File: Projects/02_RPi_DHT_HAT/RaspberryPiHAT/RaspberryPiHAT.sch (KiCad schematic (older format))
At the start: 7 parts, among them J1 Raspberry_Pi_2_3, SW1 SW_DPST, U1 DHT22

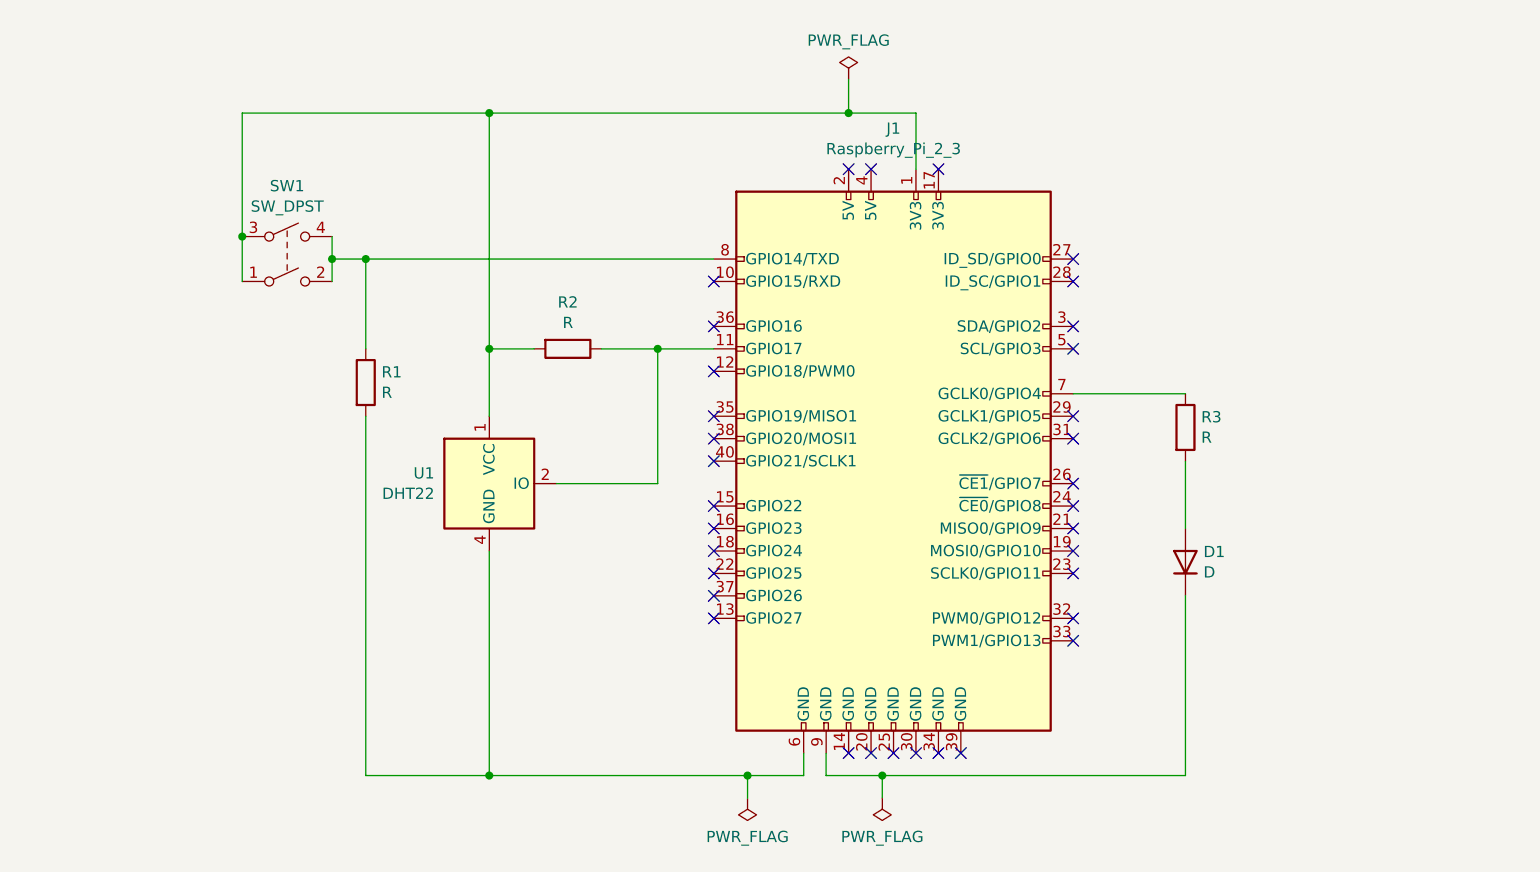
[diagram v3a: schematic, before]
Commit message: Project 2: Clean up schematic by adding common GND symbols instead of several PWR_FLAG symbols
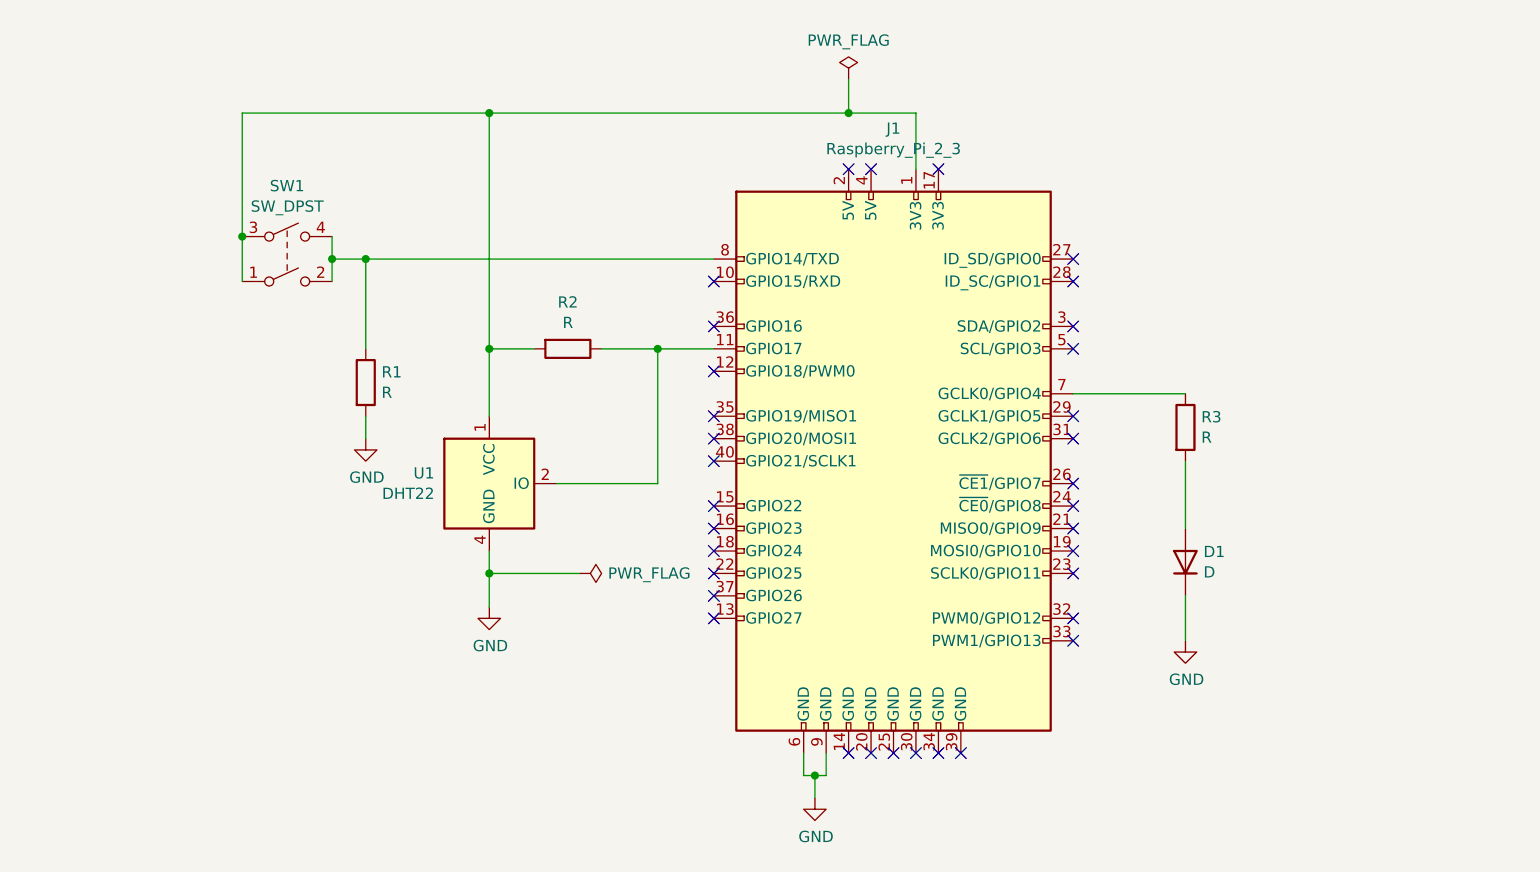
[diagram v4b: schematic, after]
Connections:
- net GND: now reaches J1.6 (GND), R1.2, U1.4 (GND)
- net GND: now also D1.1 (K), J1.9 (GND)
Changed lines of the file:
@@
 	6850 3450 6350 3450
-Wire Wire Line
-	6850 4350 6850 5150
-Wire Wire Line
-	5250 5150 5250 5050
 Wire Wire Line
 	6850 4050 6850 3750
@@
 	3200 2850 4750 2850
 Wire Wire Line
-	3200 3550 3200 5150
-Wire Wire Line
 	5150 5150 5150 5050
-Wire Wire Line
-	3750 4150 3750 5150
-Wire Wire Line
-	3200 5150 3750 5150
-Connection ~ 3750 5150
 Wire Wire Line
 	2650 2200 3750 2200
@@
 Wire Wire Line
 	5350 2200 5650 2200
+$Comp
+L power:GND #PWR0101
+U 1 1 61D42096
+P 5200 5250
+F 0 "#PWR0101" H 5200 5000 50  0001 C CNN
+F 1 "GND" H 5205 5077 50  0000 C CNN
+F 2 "" H 5200 5250 50  0001 C CNN
+F 3 "" H 5200 5250 50  0001 C CNN
+	1    5200 5250
+	1    0    0    -1
+$EndComp
 Wire Wire Line
-	3750 5150 4900 5150
+	5250 5050 5250 5150
 Wire Wire Line
-	5250 5150 5500 5150
+	5250 5150 5200 5150
+Wire Wire Line
+	5200 5150 5200 5250
+Connection ~ 5200 5150
+Wire Wire Line
+	5200 5150 5150 5150
+$Comp
+L power:GND #PWR0102
+U 1 1 61D4400F
+P 3200 3650
+F 0 "#PWR0102" H 3200 3400 50  0001 C CNN
+F 1 "GND" H 3205 3477 50  0000 C CNN
+F 2 "" H 3200 3650 50  0001 C CNN
+F 3 "" H 3200 3650 50  0001 C CNN
+	1    3200 3650
+	1    0    0    -1
+$EndComp
+$Comp
+L power:GND #PWR0103
+U 1 1 61D44D35
+P 3750 4400
+F 0 "#PWR0103" H 3750 4150 50  0001 C CNN
+F 1 "GND" H 3755 4227 50  0000 C CNN
+F 2 "" H 3750 4400 50  0001 C CNN
+F 3 "" H 3750 4400 50  0001 C CNN
+	1    3750 4400
+	1    0    0    -1
+$EndComp
+Wire Wire Line
+	3750 4150 3750 4250
+Wire Wire Line
+	3200 3550 3200 3650
+Wire Wire Line
+	3750 4250 4150 4250
+Connection ~ 3750 4250
+Wire Wire Line
+	3750 4250 3750 4400
 $Comp
 L power:PWR_FLAG #FLG0102
-U 1 1 61D3DF92
-P 4900 5250
-F 0 "#FLG0102" H 4900 5325 50  0001 C CNN
-F 1 "PWR_FLAG" H 4900 5423 50  0000 C CNN
-F 2 "" H 4900 5250 50  0001 C CNN
-F 3 "~" H 4900 5250 50  0001 C CNN
-	1    4900 5250
-	-1   0    0    1
+U 1 1 61D46AB8
+P 4150 4250
+F 0 "#FLG0102" H 4150 4325 50  0001 C CNN
+F 1 "PWR_FLAG" V 4150 4378 50  0000 L CNN
+F 2 "" H 4150 4250 50  0001 C CNN
+F 3 "~" H 4150 4250 50  0001 C CNN
+	1    4150 4250
+	0    1    1    0
+$EndComp
+$Comp
+L power:GND #PWR0104
+U 1 1 61D47197
+P 6850 4550
+F 0 "#PWR0104" H 6850 4300 50  0001 C CNN
+F 1 "GND" H 6855 4377 50  0000 C CNN
+F 2 "" H 6850 4550 50  0001 C CNN
+F 3 "" H 6850 4550 50  0001 C CNN
+	1    6850 4550
+	1    0    0    -1
 $EndComp
 Wire Wire Line
-	4900 5250 4900 5150
-Connection ~ 4900 5150
-Wire Wire Line
-	4900 5150 5150 5150
-$Comp
-L power:PWR_FLAG #FLG0103
-U 1 1 61D3EFF5
-P 5500 5250
-F 0 "#FLG0103" H 5500 5325 50  0001 C CNN
-F 1 "PWR_FLAG" H 5500 5423 50  0000 C CNN
-F 2 "" H 5500 5250 50  0001 C CNN
-F 3 "~" H 5500 5250 50  0001 C CNN
-	1    5500 5250
-	-1   0    0    1
-$EndComp
-Wire Wire Line
-	5500 5250 5500 5150
-Connection ~ 5500 5150
-Wire Wire Line
-	5500 5150 6850 5150
+	6850 4550 6850 4350
 $EndSCHEMATC

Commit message: Project 2: Clean up schematic by using net labels for power, ground, and button_input
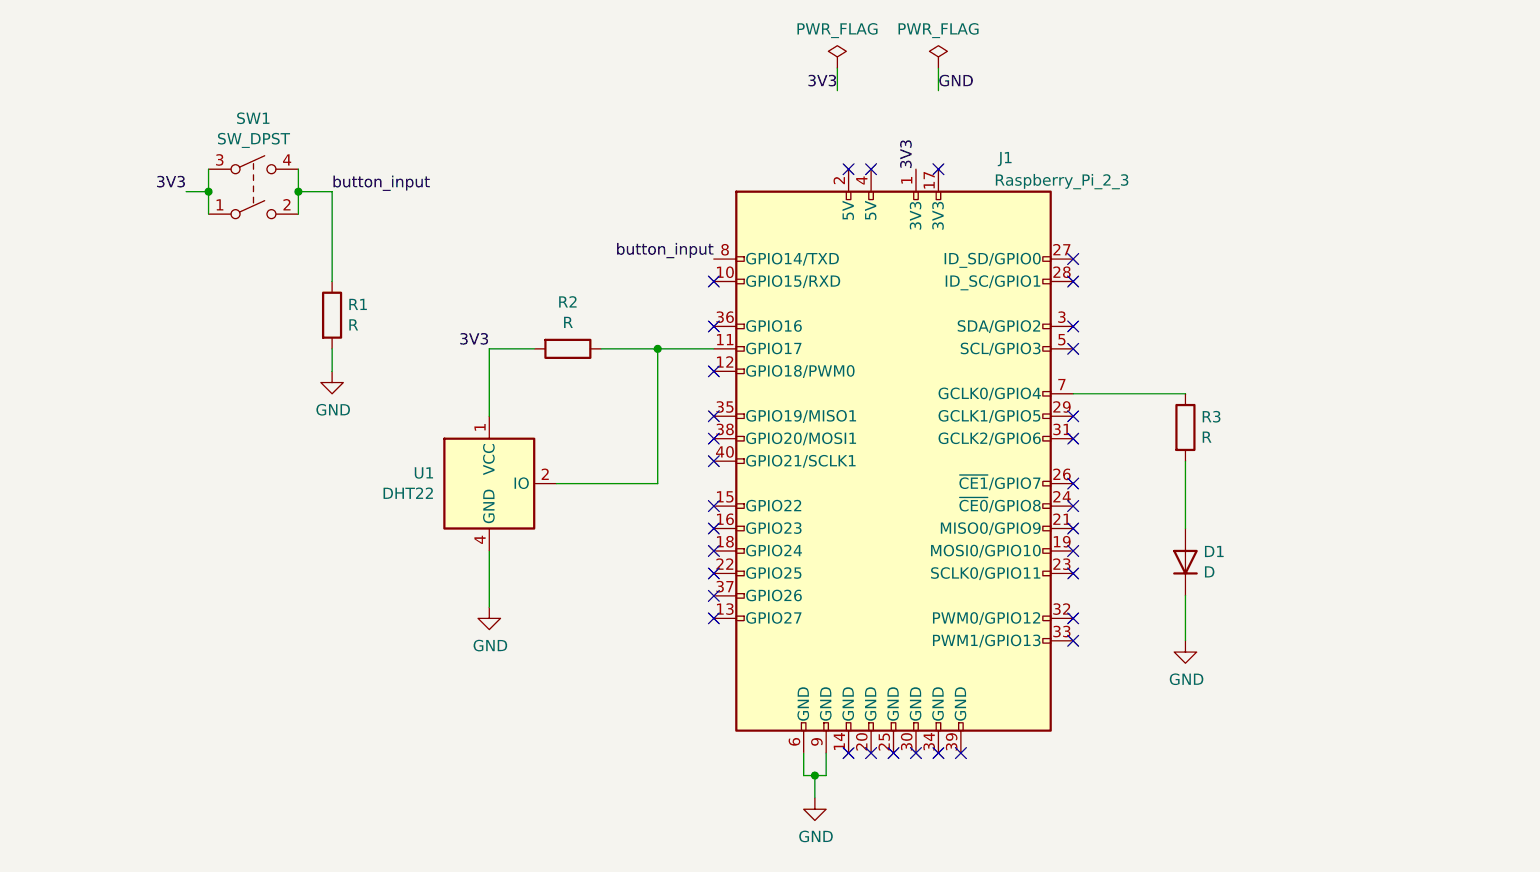
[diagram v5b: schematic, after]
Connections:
- net 3V3: now reaches J1.1 (3V3), R2.2, SW1.1, SW1.3, U1.1 (VCC)
- net button_input: now reaches J1.8 (GPIO14/TXD), R1.1, SW1.2, SW1.4
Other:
- moved on the sheet: R1, SW1
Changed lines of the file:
@@
 L Device:R R1
 U 1 1 61CFF65D
-P 3200 3400
-F 0 "R1" H 3270 3446 50  0000 L CNN
-F 1 "R" H 3270 3355 50  0000 L CNN
-F 2 "Resistor_SMD:R_0805_2012Metric" V 3130 3400 50  0001 C CNN
-F 3 "~" H 3200 3400 50  0001 C CNN
-	1    3200 3400
+P 3050 3100
+F 0 "R1" H 3120 3146 50  0000 L CNN
+F 1 "R" H 3120 3055 50  0000 L CNN
+F 2 "Resistor_SMD:R_0805_2012Metric" V 2980 3100 50  0001 C CNN
+F 3 "~" H 3050 3100 50  0001 C CNN
+	1    3050 3100
 	1    0    0    -1
 $EndComp
@@
 L Switch:SW_DPST SW1
 U 1 1 61D01499
-P 2850 2850
-F 0 "SW1" H 2850 3175 50  0000 C CNN
-F 1 "SW_DPST" H 2850 3084 50  0000 C CNN
-F 2 "freetronics_footprints:SW_PUSHBUTTON_PTH" H 2850 2850 50  0001 C CNN
-F 3 "~" H 2850 2850 50  0001 C CNN
-	1    2850 2850
+P 2700 2550
+F 0 "SW1" H 2700 2875 50  0000 C CNN
+F 1 "SW_DPST" H 2700 2784 50  0000 C CNN
+F 2 "freetronics_footprints:SW_PUSHBUTTON_PTH" H 2700 2550 50  0001 C CNN
+F 3 "~" H 2700 2550 50  0001 C CNN
+	1    2700 2550
 	1    0    0    -1
 $EndComp
@@
 U 1 1 61CF6995
 P 5550 3750
-F 0 "J1" H 5550 5231 50  0000 C CNN
-F 1 "Raspberry_Pi_2_3" H 5550 5140 50  0000 C CNN
+F 0 "J1" H 6050 5100 50  0000 C CNN
+F 1 "Raspberry_Pi_2_3" H 6300 5000 50  0000 C CNN
 F 2 "Connector_PinSocket_2.54mm:PinSocket_2x08_P2.54mm_Vertical" H 5550 3750 50  0001 C CNN
 F 3 "https://www.raspberrypi.org/documentation/hardware/raspberrypi/schematics/rpi_SCH_3bplus_1p0_reduced.pdf" H 5550 3750 50  0001 C CNN
@@
 	1    0    0    -1
 $EndComp
-Wire Wire Line
-	5650 2450 5650 2200
 $Comp
 L Device:R R2
@@
 Wire Wire Line
 	3950 3250 3750 3250
-Connection ~ 3750 3250
 Wire Wire Line
 	3750 3250 3750 3550
@@
 	4500 3250 4750 3250
 Wire Wire Line
-	3050 2750 3050 2850
-Connection ~ 3050 2850
-Wire Wire Line
-	3050 2850 3050 2950
-Wire Wire Line
-	3050 2850 3200 2850
-Wire Wire Line
-	3200 3250 3200 2850
-Connection ~ 3200 2850
-Wire Wire Line
-	3200 2850 4750 2850
+	2900 2450 2900 2550
+Connection ~ 2900 2550
+Wire Wire Line
+	2900 2550 2900 2650
+Wire Wire Line
+	2900 2550 3050 2550
+Wire Wire Line
+	3050 2950 3050 2550
 Wire Wire Line
 	5150 5150 5150 5050
 Wire Wire Line
-	2650 2200 3750 2200
-Wire Wire Line
-	2650 2200 2650 2750
-Connection ~ 2650 2750
-Wire Wire Line
-	2650 2750 2650 2950
-Wire Wire Line
-	3750 2200 3750 3250
-Connection ~ 3750 2200
-Wire Wire Line
-	3750 2200 5350 2200
+	2500 2450 2500 2550
 NoConn ~ 4750 2950
 NoConn ~ 4750 3150
@@
 NoConn ~ 5350 2450
 $Comp
-L power:PWR_FLAG #FLG0101
-U 1 1 61D30DD8
-P 5350 2050
-F 0 "#FLG0101" H 5350 2125 50  0001 C CNN
-F 1 "PWR_FLAG" H 5350 2223 50  0000 C CNN
-F 2 "" H 5350 2050 50  0001 C CNN
-F 3 "~" H 5350 2050 50  0001 C CNN
-	1    5350 2050
-	1    0    0    -1
-$EndComp
-Wire Wire Line
-	5350 2050 5350 2200
-Connection ~ 5350 2200
-Wire Wire Line
-	5350 2200 5650 2200
-$Comp
 L power:GND #PWR0101
 U 1 1 61D42096
@@
 L power:GND #PWR0102
 U 1 1 61D4400F
-P 3200 3650
-F 0 "#PWR0102" H 3200 3400 50  0001 C CNN
-F 1 "GND" H 3205 3477 50  0000 C CNN
-F 2 "" H 3200 3650 50  0001 C CNN
-F 3 "" H 3200 3650 50  0001 C CNN
-	1    3200 3650
+P 3050 3350
+F 0 "#PWR0102" H 3050 3100 50  0001 C CNN
+F 1 "GND" H 3055 3177 50  0000 C CNN
+F 2 "" H 3050 3350 50  0001 C CNN
+F 3 "" H 3050 3350 50  0001 C CNN
+	1    3050 3350
 	1    0    0    -1
 $EndComp
@@
 $EndComp
 Wire Wire Line
-	3750 4150 3750 4250
-Wire Wire Line
-	3200 3550 3200 3650
-Wire Wire Line
-	3750 4250 4150 4250
-Connection ~ 3750 4250
-Wire Wire Line
-	3750 4250 3750 4400
-$Comp
-L power:PWR_FLAG #FLG0102
-U 1 1 61D46AB8
-P 4150 4250
-F 0 "#FLG0102" H 4150 4325 50  0001 C CNN
-F 1 "PWR_FLAG" V 4150 4378 50  0000 L CNN
-F 2 "" H 4150 4250 50  0001 C CNN
-F 3 "~" H 4150 4250 50  0001 C CNN
-	1    4150 4250
-	0    1    1    0
-$EndComp
+	3050 3250 3050 3350
 $Comp
 L power:GND #PWR0104
@@
 Wire Wire Line
 	6850 4550 6850 4350
+Text Label 4750 2850 2    50   ~ 0
+button_input
+Text Label 3050 2550 0    50   ~ 0
+button_input
+Text Label 5650 2450 1    50   ~ 0
+3V3
+Text Label 3750 3250 2    50   ~ 0
+3V3
+Wire Wire Line
+	2500 2550 2400 2550
+Connection ~ 2500 2550
+Wire Wire Line
+	2500 2550 2500 2650
+Text Label 2400 2550 2    50   ~ 0
+3V3
+Wire Wire Line
+	3750 4150 3750 4400
+Text Label 5300 2100 2    50   ~ 0
+3V3
+Text Label 5750 2100 0    50   ~ 0
+GND
+Wire Wire Line
+	5750 2000 5750 2100
+Wire Wire Line
+	5300 2000 5300 2100
+$Comp
+L power:PWR_FLAG #FLG0102
+U 1 1 61D4FE8E
+P 5750 2000
+F 0 "#FLG0102" H 5750 2075 50  0001 C CNN
+F 1 "PWR_FLAG" H 5750 2173 50  0000 C CNN
+F 2 "" H 5750 2000 50  0001 C CNN
+F 3 "~" H 5750 2000 50  0001 C CNN
+	1    5750 2000
+	1    0    0    -1
+$EndComp
+$Comp
+L power:PWR_FLAG #FLG0101
+U 1 1 61D30DD8
+P 5300 2000
+F 0 "#FLG0101" H 5300 2075 50  0001 C CNN
+F 1 "PWR_FLAG" H 5300 2173 50  0000 C CNN
+F 2 "" H 5300 2000 50  0001 C CNN
+F 3 "~" H 5300 2000 50  0001 C CNN
+	1    5300 2000
+	1    0    0    -1
+$EndComp
 $EndSCHEMATC

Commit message: Project 2: Add a power LED indicator to the schematic
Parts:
- added D2: D, LED_SMD:LED_0805_2012Metric, symbol Device:D
- added R4: R, Resistor_SMD:R_0805_2012Metric, symbol Device:R
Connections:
- net 3V3: now also R4.1
- net GND: now also D2.1 (K)
- new net: D2.2 (A), R4.2
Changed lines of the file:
@@
 	0    -1   -1   0
-$EndComp
-$Comp
-L Device:R R1
-U 1 1 61CFF65D
-P 3050 3100
-F 0 "R1" H 3120 3146 50  0000 L CNN
-F 1 "R" H 3120 3055 50  0000 L CNN
-F 2 "Resistor_SMD:R_0805_2012Metric" V 2980 3100 50  0001 C CNN
-F 3 "~" H 3050 3100 50  0001 C CNN
-	1    3050 3100
-	1    0    0    -1
-$EndComp
-$Comp
-L Switch:SW_DPST SW1
-U 1 1 61D01499
-P 2700 2550
-F 0 "SW1" H 2700 2875 50  0000 C CNN
-F 1 "SW_DPST" H 2700 2784 50  0000 C CNN
-F 2 "freetronics_footprints:SW_PUSHBUTTON_PTH" H 2700 2550 50  0001 C CNN
-F 3 "~" H 2700 2550 50  0001 C CNN
-	1    2700 2550
-	1    0    0    -1
 $EndComp
 Wire Wire Line
@@
 	4500 3250 4750 3250
 Wire Wire Line
-	2900 2450 2900 2550
-Connection ~ 2900 2550
-Wire Wire Line
-	2900 2550 2900 2650
-Wire Wire Line
-	2900 2550 3050 2550
-Wire Wire Line
-	3050 2950 3050 2550
-Wire Wire Line
 	5150 5150 5150 5050
-Wire Wire Line
-	2500 2450 2500 2550
 NoConn ~ 4750 2950
 NoConn ~ 4750 3150
@@
 	5200 5150 5150 5150
 $Comp
+L power:GND #PWR0103
+U 1 1 61D44D35
+P 3750 4400
+F 0 "#PWR0103" H 3750 4150 50  0001 C CNN
+F 1 "GND" H 3755 4227 50  0000 C CNN
+F 2 "" H 3750 4400 50  0001 C CNN
+F 3 "" H 3750 4400 50  0001 C CNN
+	1    3750 4400
+	1    0    0    -1
+$EndComp
+$Comp
+L power:GND #PWR0104
+U 1 1 61D47197
+P 6850 4550
+F 0 "#PWR0104" H 6850 4300 50  0001 C CNN
+F 1 "GND" H 6855 4377 50  0000 C CNN
+F 2 "" H 6850 4550 50  0001 C CNN
+F 3 "" H 6850 4550 50  0001 C CNN
+	1    6850 4550
+	1    0    0    -1
+$EndComp
+Wire Wire Line
+	6850 4550 6850 4350
+Text Label 4750 2850 2    50   ~ 0
+button_input
+Text Label 5650 2450 1    50   ~ 0
+3V3
+Text Label 3750 3250 2    50   ~ 0
+3V3
+Wire Wire Line
+	3750 4150 3750 4400
+Text Label 7600 3450 2    50   ~ 0
+3V3
+Wire Wire Line
+	7600 4550 7600 4350
+$Comp
+L power:GND #PWR01
+U 1 1 61D00BE6
+P 7600 4550
+F 0 "#PWR01" H 7600 4300 50  0001 C CNN
+F 1 "GND" H 7605 4377 50  0000 C CNN
+F 2 "" H 7600 4550 50  0001 C CNN
+F 3 "" H 7600 4550 50  0001 C CNN
+	1    7600 4550
+	1    0    0    -1
+$EndComp
+Wire Wire Line
+	7600 4050 7600 3750
+$Comp
+L Device:D D2
+U 1 1 61D00BDA
+P 7600 4200
+F 0 "D2" V 7646 4120 50  0000 R CNN
+F 1 "D" V 7555 4120 50  0000 R CNN
+F 2 "LED_SMD:LED_0805_2012Metric" H 7600 4200 50  0001 C CNN
+F 3 "~" H 7600 4200 50  0001 C CNN
+	1    7600 4200
+	0    -1   -1   0
+$EndComp
+$Comp
+L Device:R R4
+U 1 1 61D00A50
+P 7600 3600
+F 0 "R4" H 7670 3646 50  0000 L CNN
+F 1 "R" H 7670 3555 50  0000 L CNN
+F 2 "Resistor_SMD:R_0805_2012Metric" V 7530 3600 50  0001 C CNN
+F 3 "~" H 7600 3600 50  0001 C CNN
+	1    7600 3600
+	1    0    0    -1
+$EndComp
+$Comp
+L power:PWR_FLAG #FLG0101
+U 1 1 61D30DD8
+P 5300 2000
+F 0 "#FLG0101" H 5300 2075 50  0001 C CNN
+F 1 "PWR_FLAG" H 5300 2173 50  0000 C CNN
+F 2 "" H 5300 2000 50  0001 C CNN
+F 3 "~" H 5300 2000 50  0001 C CNN
+	1    5300 2000
+	1    0    0    -1
+$EndComp
+$Comp
+L power:PWR_FLAG #FLG0102
+U 1 1 61D4FE8E
+P 5750 2000
+F 0 "#FLG0102" H 5750 2075 50  0001 C CNN
+F 1 "PWR_FLAG" H 5750 2173 50  0000 C CNN
+F 2 "" H 5750 2000 50  0001 C CNN
+F 3 "~" H 5750 2000 50  0001 C CNN
+	1    5750 2000
+	1    0    0    -1
+$EndComp
+Wire Wire Line
+	5300 2000 5300 2100
+Wire Wire Line
+	5750 2000 5750 2100
+Text Label 5750 2100 0    50   ~ 0
+GND
+Text Label 5300 2100 2    50   ~ 0
+3V3
+Text Label 2400 2550 2    50   ~ 0
+3V3
+Wire Wire Line
+	2500 2550 2500 2650
+Connection ~ 2500 2550
+Wire Wire Line
+	2500 2550 2400 2550
+Text Label 3050 2550 0    50   ~ 0
+button_input
+Wire Wire Line
+	3050 3250 3050 3350
+$Comp
 L power:GND #PWR0102
 U 1 1 61D4400F
@@
 	1    0    0    -1
 $EndComp
-$Comp
-L power:GND #PWR0103
-U 1 1 61D44D35
-P 3750 4400
-F 0 "#PWR0103" H 3750 4150 50  0001 C CNN
-F 1 "GND" H 3755 4227 50  0000 C CNN
-F 2 "" H 3750 4400 50  0001 C CNN
-F 3 "" H 3750 4400 50  0001 C CNN
-	1    3750 4400
-	1    0    0    -1
-$EndComp
-Wire Wire Line
-	3050 3250 3050 3350
-$Comp
-L power:GND #PWR0104
-U 1 1 61D47197
-P 6850 4550
-F 0 "#PWR0104" H 6850 4300 50  0001 C CNN
-F 1 "GND" H 6855 4377 50  0000 C CNN
-F 2 "" H 6850 4550 50  0001 C CNN
-F 3 "" H 6850 4550 50  0001 C CNN
-	1    6850 4550
-	1    0    0    -1
-$EndComp
-Wire Wire Line
-	6850 4550 6850 4350
-Text Label 4750 2850 2    50   ~ 0
-button_input
-Text Label 3050 2550 0    50   ~ 0
-button_input
-Text Label 5650 2450 1    50   ~ 0
-3V3
-Text Label 3750 3250 2    50   ~ 0
-3V3
-Wire Wire Line
-	2500 2550 2400 2550
-Connection ~ 2500 2550
-Wire Wire Line
-	2500 2550 2500 2650
-Text Label 2400 2550 2    50   ~ 0
-3V3
-Wire Wire Line
-	3750 4150 3750 4400
-Text Label 5300 2100 2    50   ~ 0
-3V3
-Text Label 5750 2100 0    50   ~ 0
-GND
-Wire Wire Line
-	5750 2000 5750 2100
-Wire Wire Line
-	5300 2000 5300 2100
-$Comp
-L power:PWR_FLAG #FLG0102
-U 1 1 61D4FE8E
-P 5750 2000
-F 0 "#FLG0102" H 5750 2075 50  0001 C CNN
-F 1 "PWR_FLAG" H 5750 2173 50  0000 C CNN
-F 2 "" H 5750 2000 50  0001 C CNN
-F 3 "~" H 5750 2000 50  0001 C CNN
-	1    5750 2000
-	1    0    0    -1
-$EndComp
-$Comp
-L power:PWR_FLAG #FLG0101
-U 1 1 61D30DD8
-P 5300 2000
-F 0 "#FLG0101" H 5300 2075 50  0001 C CNN
-F 1 "PWR_FLAG" H 5300 2173 50  0000 C CNN
-F 2 "" H 5300 2000 50  0001 C CNN
-F 3 "~" H 5300 2000 50  0001 C CNN
-	1    5300 2000
-	1    0    0    -1
-$EndComp
+Wire Wire Line
+	2500 2450 2500 2550
+Wire Wire Line
+	3050 2950 3050 2550
+Wire Wire Line
+	2900 2550 3050 2550
+Wire Wire Line
+	2900 2550 2900 2650
+Connection ~ 2900 2550
+Wire Wire Line
+	2900 2450 2900 2550
+$Comp
+L Switch:SW_DPST SW1
+U 1 1 61D01499
+P 2700 2550
+F 0 "SW1" H 2700 2875 50  0000 C CNN
+F 1 "SW_DPST" H 2700 2784 50  0000 C CNN
+F 2 "freetronics_footprints:SW_PUSHBUTTON_PTH" H 2700 2550 50  0001 C CNN
+F 3 "~" H 2700 2550 50  0001 C CNN
+	1    2700 2550
+	1    0    0    -1
+$EndComp
+$Comp
+L Device:R R1
+U 1 1 61CFF65D
+P 3050 3100
+F 0 "R1" H 3120 3146 50  0000 L CNN
+F 1 "R" H 3120 3055 50  0000 L CNN
+F 2 "Resistor_SMD:R_0805_2012Metric" V 2980 3100 50  0001 C CNN
+F 3 "~" H 3050 3100 50  0001 C CNN
+	1    3050 3100
+	1    0    0    -1
+$EndComp
